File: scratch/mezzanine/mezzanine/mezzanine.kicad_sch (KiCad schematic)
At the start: 5 parts, among them J101 Conn_02x20_Counter_Clockwise_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, J102 Conn_02x20_Counter_Clockwise_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, J103 Conn_02x10_Odd_Even, U101 Caravel_COB, U102 Caravel_COB

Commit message: padring v0.1
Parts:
- added U101: Caravel_COB, WafeSpace:waferspace_default_padring_v0, symbol WaferSpace:Caravel_COB
- added U103: Caravel_COB, WafeSpace:LGA2, symbol WaferSpace:Caravel_COB
- renumbered U101 to U102, U102 to U104

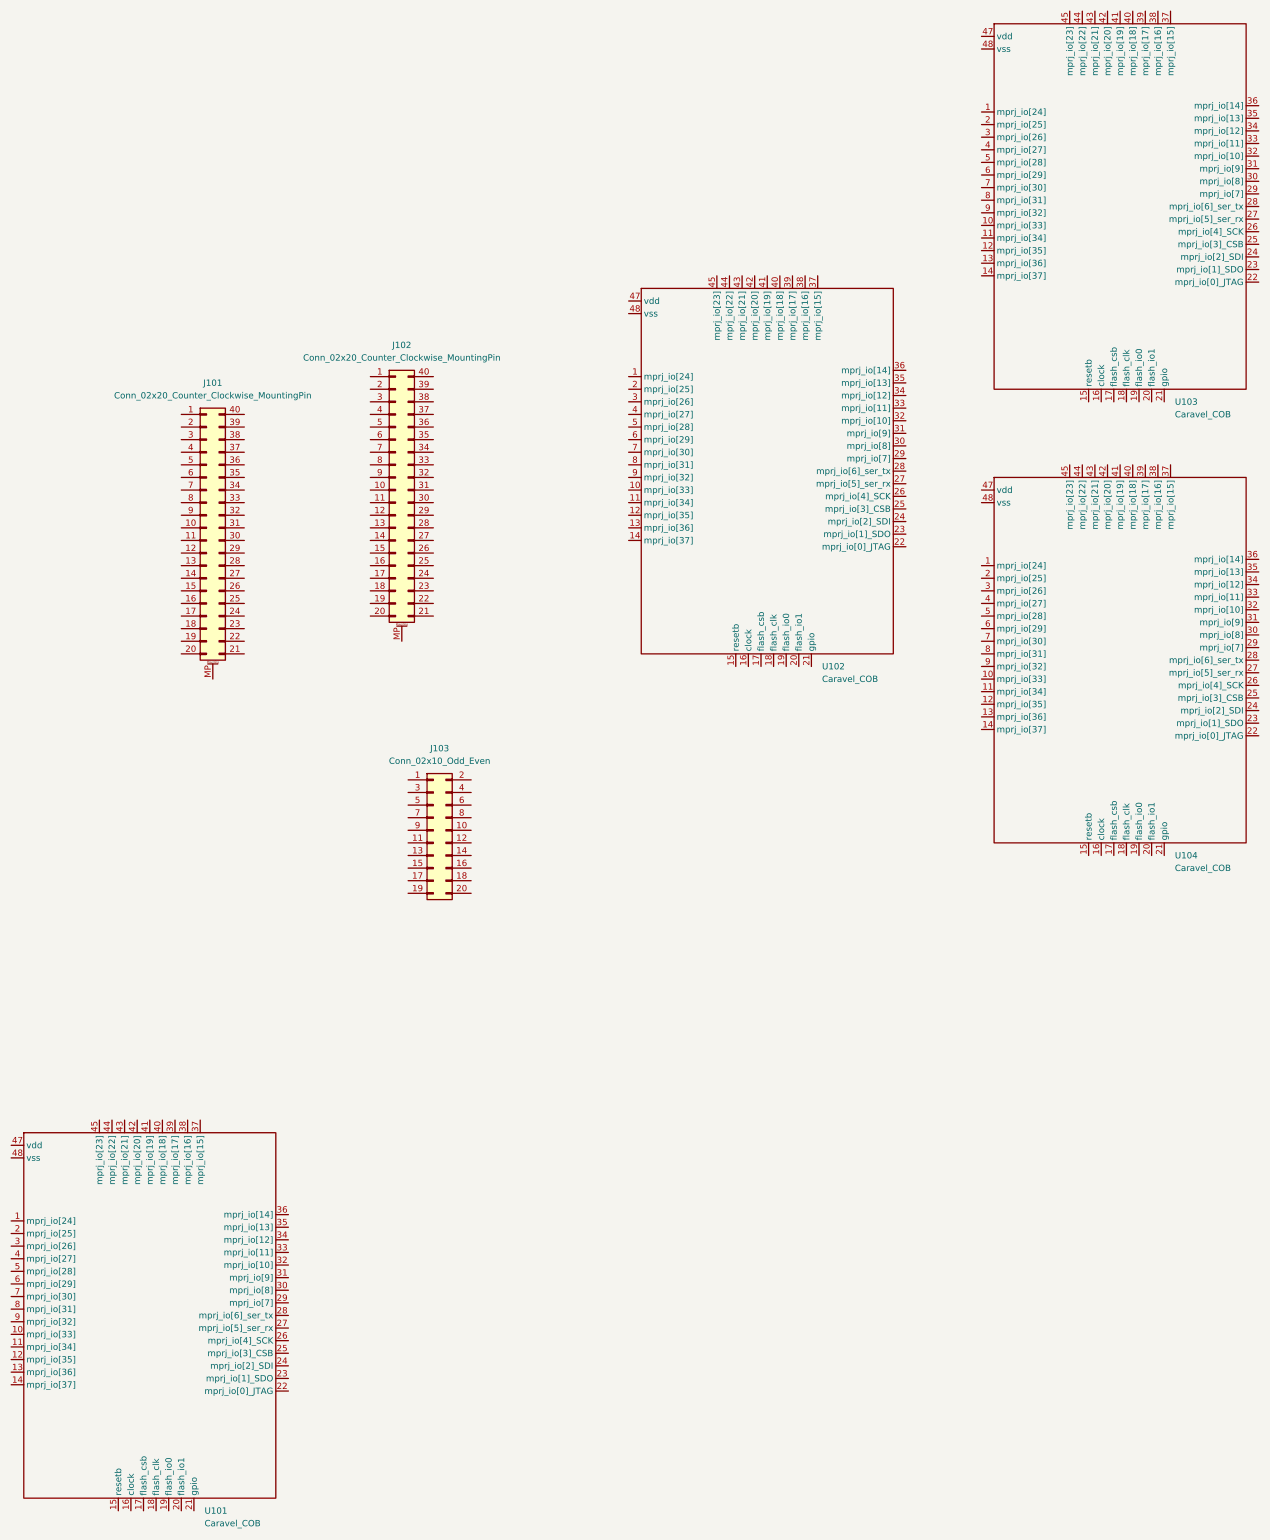
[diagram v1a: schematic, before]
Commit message: 70pin mezzanine added
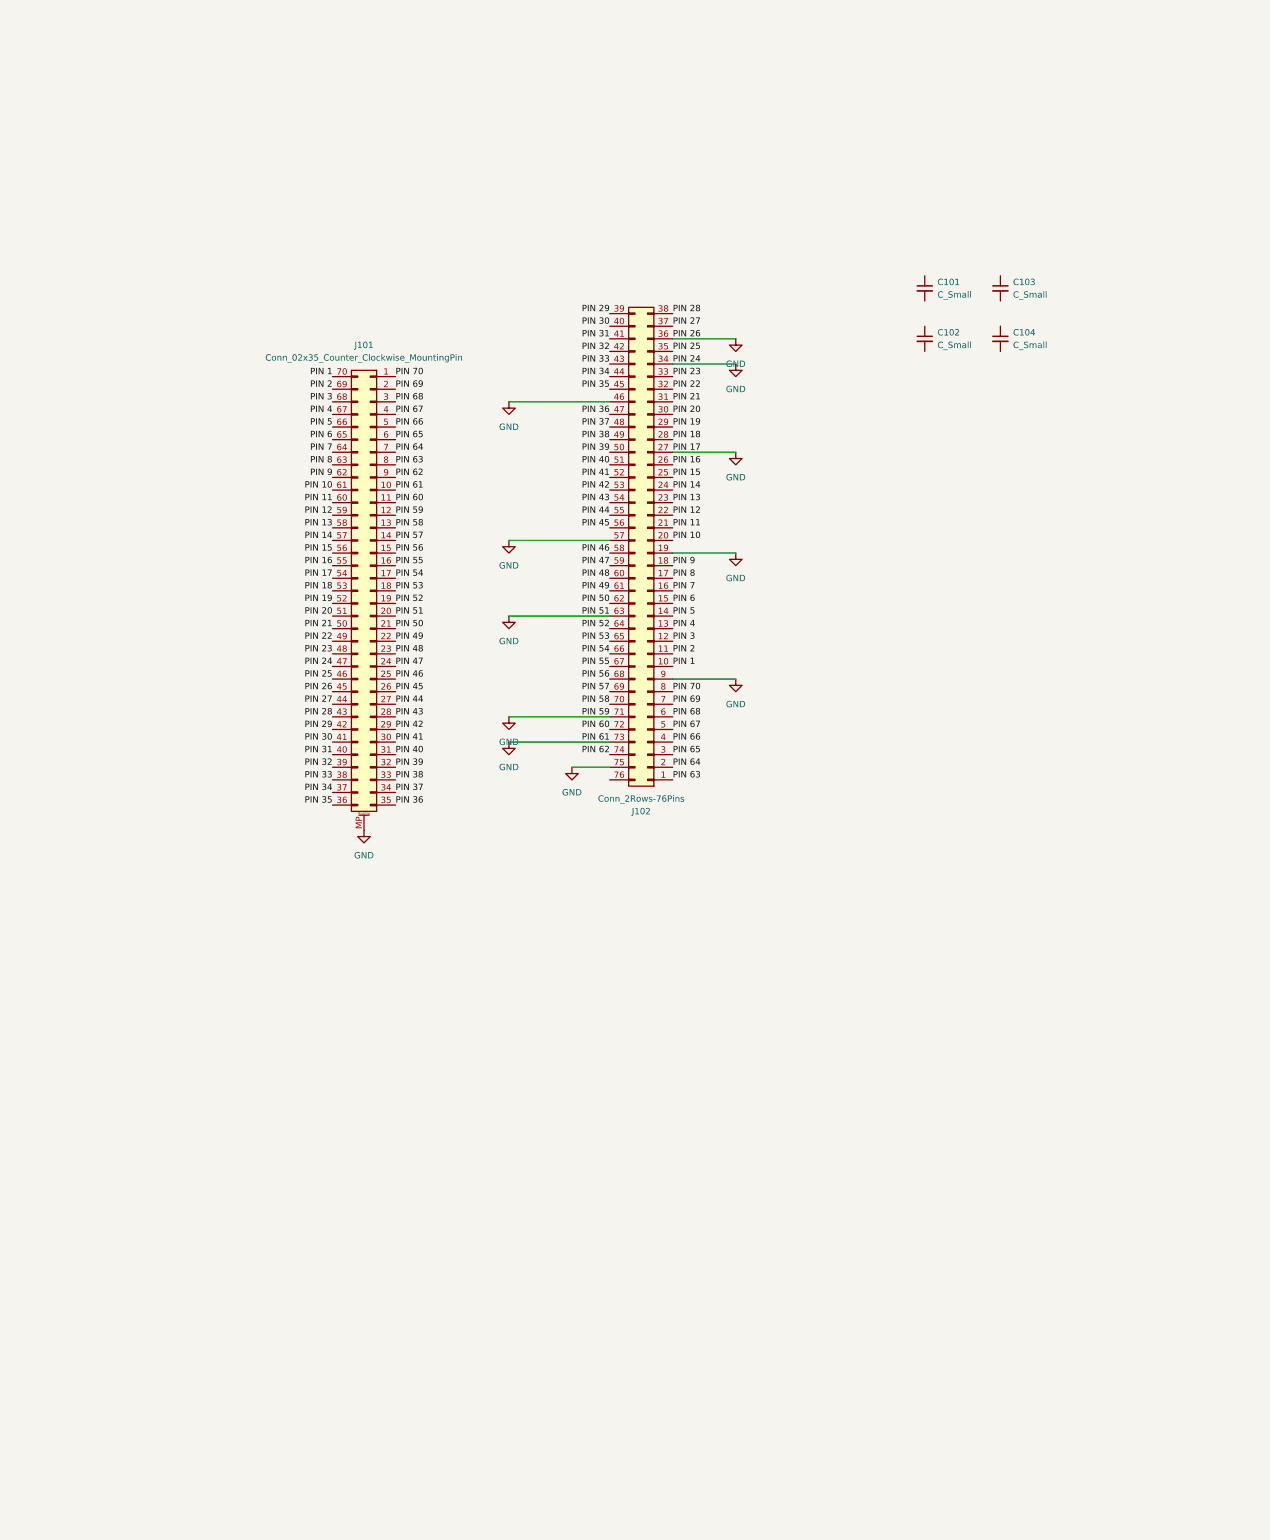
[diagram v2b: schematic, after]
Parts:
- removed J101: Conn_02x20_Counter_Clockwise_MountingPin, Connector_Mezzanine:CONN-SMD_YXT-BB10-50S-02, symbol Connector_Generic_MountingPin:Conn_02x20_Counter_Clockwise_MountingPin
- removed J102: Conn_02x20_Counter_Clockwise_MountingPin, Connector_Mezzanine:CONN-SMD_YXT-BB10-40S-02, symbol Connector_Generic_MountingPin:Conn_02x20_Counter_Clockwise_MountingPin
- removed J103: Conn_02x10_Odd_Even, Connector_PinHeader_1.27mm:PinHeader_2x19_P1.27mm_Vertical, symbol Connector_Generic:Conn_02x10_Odd_Even
- removed U101: Caravel_COB, WafeSpace:waferspace_default_padring_v0, symbol WaferSpace:Caravel_COB
- removed U102: Caravel_COB, WafeSpace:caravel_gfmpw_1_0_asap, symbol WaferSpace:Caravel_COB
- removed U103: Caravel_COB, WafeSpace:LGA2, symbol WaferSpace:Caravel_COB
- removed U104: Caravel_COB, WafeSpace:LGA1, symbol WaferSpace:Caravel_COB
- added C101, C102, C103, C104: C_Small, Capacitor_SMD:C_0201_0603Metric, symbol Device:C_Small
- added J101: Conn_02x35_Counter_Clockwise_MountingPin, Connector_Mezzanine:CONN-SMD_70P-P0.40_HCTL_HC-PBB40C-70DP-0.4V-02, symbol Connector_Generic_MountingPin:Conn_02x35_Counter_Clockwise_MountingPin
- added J102: Conn_2Rows-76Pins, WafeSpace:waferspace_default_padring_v0.2, symbol Connector_Generic:Conn_02x38_Counter_Clockwise
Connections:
- new net GND: J101.10 (Pin_10), J101.12 (Pin_12), J101.20 (Pin_20), J101.45 (Pin_45), J101.47 (Pin_47), J101.54 (Pin_54), J101.MP (MountPin), J102.19 (Pin_19), J102.27 (Pin_27), J102.34 (Pin_34), J102.36 (Pin_36), J102.46 (Pin_46), J102.57 (Pin_57), J102.63 (Pin_63), J102.71 (Pin_71), J102.73 (Pin_73), J102.75 (Pin_75), J102.9 (Pin_9)
- new net PIN 1: J101.70 (Pin_70), J102.10 (Pin_10)
- new net PIN 10: J101.61 (Pin_61), J102.20 (Pin_20)
- new net PIN 11: J101.60 (Pin_60), J102.21 (Pin_21)
- new net PIN 12: J101.59 (Pin_59), J102.22 (Pin_22)
- new net PIN 13: J101.58 (Pin_58), J102.23 (Pin_23)
- new net PIN 14: J101.57 (Pin_57), J102.24 (Pin_24)
- new net PIN 15: J101.56 (Pin_56), J102.25 (Pin_25)
- new net PIN 16: J101.55 (Pin_55), J102.26 (Pin_26)
- new net PIN 18: J101.53 (Pin_53), J102.28 (Pin_28)
- new net PIN 19: J101.52 (Pin_52), J102.29 (Pin_29)
- new net PIN 2: J101.69 (Pin_69), J102.11 (Pin_11)
- new net PIN 20: J101.51 (Pin_51), J102.30 (Pin_30)
- new net PIN 21: J101.50 (Pin_50), J102.31 (Pin_31)
- new net PIN 22: J101.49 (Pin_49), J102.32 (Pin_32)
- new net PIN 23: J101.48 (Pin_48), J102.33 (Pin_33)
- new net PIN 25: J101.46 (Pin_46), J102.35 (Pin_35)
- new net PIN 27: J101.44 (Pin_44), J102.37 (Pin_37)
- new net PIN 28: J101.43 (Pin_43), J102.38 (Pin_38)
- new net PIN 29: J101.42 (Pin_42), J102.39 (Pin_39)
- new net PIN 3: J101.68 (Pin_68), J102.12 (Pin_12)
- new net PIN 30: J101.41 (Pin_41), J102.40 (Pin_40)
- new net PIN 31: J101.40 (Pin_40), J102.41 (Pin_41)
- new net PIN 32: J101.39 (Pin_39), J102.42 (Pin_42)
- new net PIN 33: J101.38 (Pin_38), J102.43 (Pin_43)
- new net PIN 34: J101.37 (Pin_37), J102.44 (Pin_44)
- new net PIN 35: J101.36 (Pin_36), J102.45 (Pin_45)
- new net PIN 36: J101.35 (Pin_35), J102.47 (Pin_47)
- new net PIN 37: J101.34 (Pin_34), J102.48 (Pin_48)
- new net PIN 38: J101.33 (Pin_33), J102.49 (Pin_49)
- new net PIN 39: J101.32 (Pin_32), J102.50 (Pin_50)
- new net PIN 4: J101.67 (Pin_67), J102.13 (Pin_13)
- new net PIN 40: J101.31 (Pin_31), J102.51 (Pin_51)
- new net PIN 41: J101.30 (Pin_30), J102.52 (Pin_52)
- new net PIN 42: J101.29 (Pin_29), J102.53 (Pin_53)
- new net PIN 43: J101.28 (Pin_28), J102.54 (Pin_54)
- new net PIN 44: J101.27 (Pin_27), J102.55 (Pin_55)
- new net PIN 45: J101.26 (Pin_26), J102.56 (Pin_56)
- new net PIN 46: J101.25 (Pin_25), J102.58 (Pin_58)
- new net PIN 47: J101.24 (Pin_24), J102.59 (Pin_59)
- new net PIN 48: J101.23 (Pin_23), J102.60 (Pin_60)
- new net PIN 49: J101.22 (Pin_22), J102.61 (Pin_61)
- new net PIN 5: J101.66 (Pin_66), J102.14 (Pin_14)
- new net PIN 50: J101.21 (Pin_21), J102.62 (Pin_62)
- new net PIN 52: J101.19 (Pin_19), J102.64 (Pin_64)
- new net PIN 53: J101.18 (Pin_18), J102.65 (Pin_65)
- new net PIN 54: J101.17 (Pin_17), J102.66 (Pin_66)
- new net PIN 55: J101.16 (Pin_16), J102.67 (Pin_67)
- new net PIN 56: J101.15 (Pin_15), J102.68 (Pin_68)
- new net PIN 57: J101.14 (Pin_14), J102.69 (Pin_69)
- new net PIN 58: J101.13 (Pin_13), J102.70 (Pin_70)
- new net PIN 6: J101.65 (Pin_65), J102.15 (Pin_15)
- new net PIN 60: J101.11 (Pin_11), J102.72 (Pin_72)
- new net PIN 62: J101.9 (Pin_9), J102.74 (Pin_74)
- new net PIN 63: J101.8 (Pin_8), J102.1 (Pin_1)
- new net PIN 64: J101.7 (Pin_7), J102.2 (Pin_2)
- new net PIN 65: J101.6 (Pin_6), J102.3 (Pin_3)
- new net PIN 66: J101.5 (Pin_5), J102.4 (Pin_4)
- new net PIN 67: J101.4 (Pin_4), J102.5 (Pin_5)
- new net PIN 68: J101.3 (Pin_3), J102.6 (Pin_6)
- new net PIN 69: J101.2 (Pin_2), J102.7 (Pin_7)
- new net PIN 7: J101.64 (Pin_64), J102.16 (Pin_16)
- new net PIN 70: J101.1 (Pin_1), J102.8 (Pin_8)
- new net PIN 8: J101.63 (Pin_63), J102.17 (Pin_17)
- new net PIN 9: J101.62 (Pin_62), J102.18 (Pin_18)
